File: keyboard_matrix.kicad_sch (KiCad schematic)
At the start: 208 parts

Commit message: Rename switch refdes
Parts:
- renumbered K_0 to SW2000, K_1 to SW2001, K_2 to SW2002, K_3 to SW2003, K_4 to SW2004, K_5 to SW2005, K_6 to SW2006, K_7 to SW2007, K_8 to SW2008, K_9 to SW2009, K_10 to SW2010, K_11 to SW2011, K_12 to SW2012, K_13 to SW2013, K_14 to SW2014, K_15 to SW2015, K_16 to SW2016, K_17 to SW2017, K_18 to SW2018, K_19 to SW2019, K_20 to SW2020, K_21 to SW2021, K_22 to SW2022, K_23 to SW2023, K_24 to SW2024, K_25 to SW2025, K_26 to SW2026, K_27 to SW2027, K_28 to SW2028, K_29 to SW2029, K_30 to SW2030, K_31 to SW2031, K_32 to SW2032, K_33 to SW2033, K_34 to SW2034, K_35 to SW2035, K_36 to SW2036, K_37 to SW2037, K_38 to SW2038, K_39 to SW2039, K_40 to SW2040, K_41 to SW2041, K_42 to SW2042, K_43 to SW2043, K_44 to SW2044, K_45 to SW2045, K_46 to SW2046, K_47 to SW2047, K_48 to SW2048, K_49 to SW2049, K_50 to SW2050, K_51 to SW2051, K_52 to SW2052, K_53 to SW2053, K_54 to SW2054, K_55 to SW2055, K_56 to SW2056, K_57 to SW2057, K_58 to SW2058, K_59 to SW2059, K_60 to SW2060, K_61 to SW2061, K_62 to SW2062, K_63 to SW2063, K_64 to SW2064, K_65 to SW2065, K_66 to SW2066, K_67 to SW2067, K_68 to SW2068, K_69 to SW2069, K_70 to SW2070, K_71 to SW2071, K_72 to SW2072, K_73 to SW2073, K_74 to SW2074, K_75 to SW2075, K_76 to SW2076, K_77 to SW2077, K_78 to SW2078, K_79 to SW2079, K_80 to SW2080, K_81 to SW2081, K_82 to SW2082, K_83 to SW2083, K_84 to SW2084, K_85 to SW2085, K_86 to SW2086, K_87 to SW2087, K_88 to SW2088, K_89 to SW2089, K_90 to SW2090, K_91 to SW2091, K_92 to SW2092, K_93 to SW2093, K_94 to SW2094, K_95 to SW2095, K_96 to SW2096, K_97 to SW2097, K_98 to SW2098, K_99 to SW2099, K_100 to SW2100, K_101 to SW2101, K_102 to SW2102, K_103 to SW2103

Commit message: Working towards SMD LEDs
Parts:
- added unit 2 of SW2000
- added SW? (x73): MX-LED, symbol Keyboard:MX-LED
- SW2000: value Esc -> MX-LED; footprint Keyboard:MXOnly-1U-Hotswap -> (none)
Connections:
- net G0: now also SW2000.4 (G), SW?.4 (G), SW?.4 (G), SW?.4 (G), SW?.4 (G), SW?.4 (G), SW?.4 (G), SW?.4 (G), SW?.4 (G), SW?.4 (G), SW?.4 (G), SW?.4 (G), SW?.4 (G), SW?.4 (G), SW?.4 (G), SW?.4 (G), SW?.4 (G), SW?.4 (G), SW?.4 (G), SW?.4 (G), SW?.4 (G), SW?.4 (G), SW?.4 (G), SW?.4 (G), SW?.4 (G), SW?.4 (G), SW?.4 (G), SW?.4 (G), SW?.4 (G), SW?.4 (G), SW?.4 (G), SW?.4 (G), SW?.4 (G), SW?.4 (G), SW?.4 (G), SW?.4 (G), SW?.4 (G), SW?.4 (G), SW?.4 (G), SW?.4 (G), SW?.4 (G), SW?.4 (G), SW?.4 (G), SW?.4 (G), SW?.4 (G), SW?.4 (G), SW?.4 (G), SW?.4 (G), SW?.4 (G), SW?.4 (G), SW?.4 (G), SW?.4 (G), SW?.4 (G), SW?.4 (G), SW?.4 (G), SW?.4 (G), SW?.4 (G), SW?.4 (G), SW?.4 (G), SW?.4 (G), SW?.4 (G), SW?.4 (G), SW?.4 (G), SW?.4 (G), SW?.4 (G), SW?.4 (G), SW?.4 (G), SW?.4 (G), SW?.4 (G), SW?.4 (G), SW?.4 (G), SW?.4 (G), SW?.4 (G), SW?.4 (G); no longer SW2000.4 (LEDGND)
- net LED36: no longer SW2036.3 (LED)
- net LED57: no longer SW2057.3 (LED)
- net LED90: no longer SW2090.3 (LED)
- net LED95: no longer SW2095.3 (LED)
- net row1: no longer D_17.1 (K)
- net row4: no longer D_74.1 (K)
- net row5: no longer D_92.1 (K)
- net at D_76.2 (A): no longer SW2076.2 (ROW)
- net at SW2019.2 (ROW): no longer D_19.2 (A)
- net at D_92.2 (A): no longer SW2092.2 (ROW)
- net at SW2074.2 (ROW): no longer D_74.2 (A)
- net at SW2059.2 (ROW): no longer D_59.2 (A)
- net at SW2018.2 (ROW): no longer D_18.2 (A)
- net at SW2038.2 (ROW): no longer D_38.2 (A)
- net at D_93.2 (A): no longer SW2093.2 (ROW)
- net at D_1.2 (A): no longer SW2001.2 (ROW)
- net at SW2017.2 (ROW): no longer D_17.2 (A)
- net at SW2039.2 (ROW): no longer D_39.2 (A)
- net at D_2.2 (A): no longer SW2002.2 (ROW)
- net at SW2060.2 (ROW): no longer D_60.2 (A)
- net at D_75.2 (A): no longer SW2075.2 (ROW)
- removed net G1: SW2001.4 (LEDGND)
- removed net G10: SW2010.4 (LEDGND)
- removed net G100: SW2100.4 (LEDGND)
- removed net G101: SW2101.4 (LEDGND)
- removed net G102: SW2102.4 (LEDGND)
- removed net G103: SW2103.4 (LEDGND)
- removed net G11: SW2011.4 (LEDGND)
- removed net G12: SW2012.4 (LEDGND)
- removed net G13: SW2013.4 (LEDGND)
- removed net G14: SW2014.4 (LEDGND)
- removed net G15: SW2015.4 (LEDGND)
- removed net G16: SW2016.4 (LEDGND)
- removed net G17: SW2017.4 (LEDGND)
- removed net G18: SW2018.4 (LEDGND)
- removed net G19: SW2019.4 (LEDGND)
- removed net G2: SW2002.4 (LEDGND)
- removed net G20: SW2020.4 (LEDGND)
- removed net G21: SW2021.4 (LEDGND)
- removed net G22: SW2022.4 (LEDGND)
- removed net G23: SW2023.4 (LEDGND)
- removed net G24: SW2024.4 (LEDGND)
- removed net G25: SW2025.4 (LEDGND)
- removed net G26: SW2026.4 (LEDGND)
- removed net G27: SW2027.4 (LEDGND)
- removed net G28: SW2028.4 (LEDGND)
- removed net G29: SW2029.4 (LEDGND)
- removed net G3: SW2003.4 (LEDGND)
- removed net G30: SW2030.4 (LEDGND)
- removed net G31: SW2031.4 (LEDGND)
- removed net G32: SW2032.4 (LEDGND)
- removed net G33: SW2033.4 (LEDGND)
- removed net G34: SW2034.4 (LEDGND)
- removed net G35: SW2035.4 (LEDGND)
- removed net G36: SW2036.4 (LEDGND)
- removed net G37: SW2037.4 (LEDGND)
- removed net G38: SW2038.4 (LEDGND)
- removed net G39: SW2039.4 (LEDGND)
- removed net G4: SW2004.4 (LEDGND)
- removed net G40: SW2040.4 (LEDGND)
- removed net G41: SW2041.4 (LEDGND)
- removed net G42: SW2042.4 (LEDGND)
- removed net G43: SW2043.4 (LEDGND)
- removed net G44: SW2044.4 (LEDGND)
- removed net G45: SW2045.4 (LEDGND)
- removed net G46: SW2046.4 (LEDGND)
- removed net G47: SW2047.4 (LEDGND)
- removed net G48: SW2048.4 (LEDGND)
- removed net G49: SW2049.4 (LEDGND)
- removed net G5: SW2005.4 (LEDGND)
- removed net G50: SW2050.4 (LEDGND)
- removed net G51: SW2051.4 (LEDGND)
- removed net G52: SW2052.4 (LEDGND)
- removed net G53: SW2053.4 (LEDGND)
- removed net G54: SW2054.4 (LEDGND)
- removed net G55: SW2055.4 (LEDGND)
- removed net G56: SW2056.4 (LEDGND)
- removed net G57: SW2057.4 (LEDGND)
- removed net G58: SW2058.4 (LEDGND)
- removed net G59: SW2059.4 (LEDGND)
- removed net G6: SW2006.4 (LEDGND)
- removed net G60: SW2060.4 (LEDGND)
- removed net G61: SW2061.4 (LEDGND)
- removed net G62: SW2062.4 (LEDGND)
- removed net G63: SW2063.4 (LEDGND)
- removed net G64: SW2064.4 (LEDGND)
- removed net G65: SW2065.4 (LEDGND)
- removed net G66: SW2066.4 (LEDGND)
- removed net G67: SW2067.4 (LEDGND)
- removed net G68: SW2068.4 (LEDGND)
- removed net G69: SW2069.4 (LEDGND)
- removed net G7: SW2007.4 (LEDGND)
- removed net G70: SW2070.4 (LEDGND)
- removed net G71: SW2071.4 (LEDGND)
- removed net G72: SW2072.4 (LEDGND)
- removed net G73: SW2073.4 (LEDGND)
- removed net G74: SW2074.4 (LEDGND)
- removed net G75: SW2075.4 (LEDGND)
- removed net G76: SW2076.4 (LEDGND)
- removed net G77: SW2077.4 (LEDGND)
- removed net G78: SW2078.4 (LEDGND)
- removed net G79: SW2079.4 (LEDGND)
- removed net G8: SW2008.4 (LEDGND)
- removed net G80: SW2080.4 (LEDGND)
- removed net G81: SW2081.4 (LEDGND)
- removed net G82: SW2082.4 (LEDGND)
- removed net G83: SW2083.4 (LEDGND)
- removed net G84: SW2084.4 (LEDGND)
- removed net G85: SW2085.4 (LEDGND)
- removed net G86: SW2086.4 (LEDGND)
- removed net G87: SW2087.4 (LEDGND)
- removed net G88: SW2088.4 (LEDGND)
- removed net G89: SW2089.4 (LEDGND)
- removed net G9: SW2009.4 (LEDGND)
- removed net G90: SW2090.4 (LEDGND)
- removed net G91: SW2091.4 (LEDGND)
- removed net G92: SW2092.4 (LEDGND)
- removed net G93: SW2093.4 (LEDGND)
- removed net G94: SW2094.4 (LEDGND)
- removed net G95: SW2095.4 (LEDGND)
- removed net G96: SW2096.4 (LEDGND)
- removed net G97: SW2097.4 (LEDGND)
- removed net G98: SW2098.4 (LEDGND)
- removed net G99: SW2099.4 (LEDGND)
- removed net LED0: SW2000.3 (LED)
- removed net LED1: SW2001.3 (LED)
- removed net LED10: SW2010.3 (LED)
- removed net LED100: SW2100.3 (LED)
- removed net LED101: SW2101.3 (LED)
- removed net LED102: SW2102.3 (LED)
- removed net LED103: SW2103.3 (LED)
- removed net LED11: SW2011.3 (LED)
- removed net LED12: SW2012.3 (LED)
- removed net LED13: SW2013.3 (LED)
- removed net LED14: SW2014.3 (LED)
- removed net LED15: SW2015.3 (LED)
- removed net LED16: SW2016.3 (LED)
- removed net LED17: SW2017.3 (LED)
- removed net LED18: SW2018.3 (LED)
- removed net LED19: SW2019.3 (LED)
- removed net LED2: SW2002.3 (LED)
- removed net LED20: SW2020.3 (LED)
- removed net LED21: SW2021.3 (LED)
- removed net LED22: SW2022.3 (LED)
- removed net LED23: SW2023.3 (LED)
- removed net LED24: SW2024.3 (LED)
- removed net LED25: SW2025.3 (LED)
- removed net LED26: SW2026.3 (LED)
- removed net LED27: SW2027.3 (LED)
- removed net LED28: SW2028.3 (LED)
- removed net LED29: SW2029.3 (LED)
- removed net LED3: SW2003.3 (LED)
- removed net LED30: SW2030.3 (LED)
- removed net LED31: SW2031.3 (LED)
- removed net LED32: SW2032.3 (LED)
- removed net LED33: SW2033.3 (LED)
- removed net LED34: SW2034.3 (LED)
- removed net LED35: SW2035.3 (LED)
- removed net LED37: SW2037.3 (LED)
- removed net LED38: SW2038.3 (LED)
- removed net LED39: SW2039.3 (LED)
- removed net LED4: SW2004.3 (LED)
- removed net LED40: SW2040.3 (LED)
- removed net LED41: SW2041.3 (LED)
- removed net LED42: SW2042.3 (LED)
- removed net LED43: SW2043.3 (LED)
- removed net LED44: SW2044.3 (LED)
- removed net LED45: SW2045.3 (LED)
- removed net LED46: SW2046.3 (LED)
- removed net LED47: SW2047.3 (LED)
- removed net LED48: SW2048.3 (LED)
- removed net LED49: SW2049.3 (LED)
- removed net LED5: SW2005.3 (LED)
- removed net LED50: SW2050.3 (LED)
- removed net LED51: SW2051.3 (LED)
- removed net LED52: SW2052.3 (LED)
- removed net LED53: SW2053.3 (LED)
- removed net LED54: SW2054.3 (LED)
- removed net LED55: SW2055.3 (LED)
- removed net LED56: SW2056.3 (LED)
- removed net LED58: SW2058.3 (LED)
- removed net LED59: SW2059.3 (LED)
- removed net LED6: SW2006.3 (LED)
- removed net LED60: SW2060.3 (LED)
- removed net LED61: SW2061.3 (LED)
- removed net LED62: SW2062.3 (LED)
- removed net LED63: SW2063.3 (LED)
- removed net LED64: SW2064.3 (LED)
- removed net LED65: SW2065.3 (LED)
- removed net LED66: SW2066.3 (LED)
- removed net LED67: SW2067.3 (LED)
- removed net LED68: SW2068.3 (LED)
- removed net LED69: SW2069.3 (LED)
- removed net LED7: SW2007.3 (LED)
- removed net LED70: SW2070.3 (LED)
- removed net LED71: SW2071.3 (LED)
- removed net LED72: SW2072.3 (LED)
- removed net LED73: SW2073.3 (LED)
- removed net LED74: SW2074.3 (LED)
- removed net LED75: SW2075.3 (LED)
- removed net LED76: SW2076.3 (LED)
- removed net LED77: SW2077.3 (LED)
- removed net LED78: SW2078.3 (LED)
- removed net LED79: SW2079.3 (LED)
- removed net LED8: SW2008.3 (LED)
- removed net LED80: SW2080.3 (LED)
- removed net LED81: SW2081.3 (LED)
- removed net LED82: SW2082.3 (LED)
- removed net LED83: SW2083.3 (LED)
- removed net LED84: SW2084.3 (LED)
- removed net LED85: SW2085.3 (LED)
- removed net LED86: SW2086.3 (LED)
- removed net LED87: SW2087.3 (LED)
- removed net LED88: SW2088.3 (LED)
- removed net LED89: SW2089.3 (LED)
- removed net LED9: SW2009.3 (LED)
- removed net LED91: SW2091.3 (LED)
- removed net LED92: SW2092.3 (LED)
- removed net LED93: SW2093.3 (LED)
- removed net LED94: SW2094.3 (LED)
- removed net LED96: SW2096.3 (LED)
- removed net LED97: SW2097.3 (LED)
- removed net LED98: SW2098.3 (LED)
- removed net LED99: SW2099.3 (LED)
- new net B0: SW2000.5 (B), SW?.5 (B), SW?.5 (B), SW?.5 (B), SW?.5 (B), SW?.5 (B), SW?.5 (B), SW?.5 (B), SW?.5 (B), SW?.5 (B), SW?.5 (B), SW?.5 (B), SW?.5 (B), SW?.5 (B), SW?.5 (B), SW?.5 (B), SW?.5 (B), SW?.5 (B), SW?.5 (B), SW?.5 (B), SW?.5 (B), SW?.5 (B), SW?.5 (B), SW?.5 (B), SW?.5 (B), SW?.5 (B), SW?.5 (B), SW?.5 (B), SW?.5 (B), SW?.5 (B), SW?.5 (B), SW?.5 (B), SW?.5 (B), SW?.5 (B), SW?.5 (B), SW?.5 (B), SW?.5 (B), SW?.5 (B), SW?.5 (B), SW?.5 (B), SW?.5 (B), SW?.5 (B), SW?.5 (B), SW?.5 (B), SW?.5 (B), SW?.5 (B), SW?.5 (B), SW?.5 (B), SW?.5 (B), SW?.5 (B), SW?.5 (B), SW?.5 (B), SW?.5 (B), SW?.5 (B), SW?.5 (B), SW?.5 (B), SW?.5 (B), SW?.5 (B), SW?.5 (B), SW?.5 (B), SW?.5 (B), SW?.5 (B), SW?.5 (B), SW?.5 (B), SW?.5 (B), SW?.5 (B), SW?.5 (B), SW?.5 (B), SW?.5 (B), SW?.5 (B), SW?.5 (B), SW?.5 (B), SW?.5 (B), SW?.5 (B)
- new net COM: SW2000.6 (COM), SW?.6 (COM), SW?.6 (COM), SW?.6 (COM), SW?.6 (COM), SW?.6 (COM), SW?.6 (COM), SW?.6 (COM), SW?.6 (COM), SW?.6 (COM), SW?.6 (COM), SW?.6 (COM), SW?.6 (COM), SW?.6 (COM), SW?.6 (COM), SW?.6 (COM), SW?.6 (COM), SW?.6 (COM), SW?.6 (COM), SW?.6 (COM), SW?.6 (COM), SW?.6 (COM), SW?.6 (COM), SW?.6 (COM), SW?.6 (COM), SW?.6 (COM), SW?.6 (COM), SW?.6 (COM), SW?.6 (COM), SW?.6 (COM), SW?.6 (COM), SW?.6 (COM), SW?.6 (COM), SW?.6 (COM), SW?.6 (COM), SW?.6 (COM), SW?.6 (COM), SW?.6 (COM), SW?.6 (COM), SW?.6 (COM), SW?.6 (COM), SW?.6 (COM), SW?.6 (COM), SW?.6 (COM), SW?.6 (COM), SW?.6 (COM), SW?.6 (COM), SW?.6 (COM), SW?.6 (COM), SW?.6 (COM), SW?.6 (COM), SW?.6 (COM), SW?.6 (COM), SW?.6 (COM), SW?.6 (COM), SW?.6 (COM), SW?.6 (COM), SW?.6 (COM), SW?.6 (COM), SW?.6 (COM), SW?.6 (COM), SW?.6 (COM), SW?.6 (COM), SW?.6 (COM), SW?.6 (COM), SW?.6 (COM), SW?.6 (COM), SW?.6 (COM), SW?.6 (COM), SW?.6 (COM), SW?.6 (COM), SW?.6 (COM), SW?.6 (COM), SW?.6 (COM)
- new net R0: SW2000.3 (R), SW?.3 (R), SW?.3 (R), SW?.3 (R), SW?.3 (R), SW?.3 (R), SW?.3 (R), SW?.3 (R), SW?.3 (R), SW?.3 (R), SW?.3 (R), SW?.3 (R), SW?.3 (R), SW?.3 (R), SW?.3 (R), SW?.3 (R), SW?.3 (R), SW?.3 (R), SW?.3 (R), SW?.3 (R), SW?.3 (R), SW?.3 (R), SW?.3 (R), SW?.3 (R), SW?.3 (R), SW?.3 (R), SW?.3 (R), SW?.3 (R), SW?.3 (R), SW?.3 (R), SW?.3 (R), SW?.3 (R), SW?.3 (R), SW?.3 (R), SW?.3 (R), SW?.3 (R), SW?.3 (R), SW?.3 (R), SW?.3 (R), SW?.3 (R), SW?.3 (R), SW?.3 (R), SW?.3 (R), SW?.3 (R), SW?.3 (R), SW?.3 (R), SW?.3 (R), SW?.3 (R), SW?.3 (R), SW?.3 (R), SW?.3 (R), SW?.3 (R), SW?.3 (R), SW?.3 (R), SW?.3 (R), SW?.3 (R), SW?.3 (R), SW?.3 (R), SW?.3 (R), SW?.3 (R), SW?.3 (R), SW?.3 (R), SW?.3 (R), SW?.3 (R), SW?.3 (R), SW?.3 (R), SW?.3 (R), SW?.3 (R), SW?.3 (R), SW?.3 (R), SW?.3 (R), SW?.3 (R), SW?.3 (R), SW?.3 (R)

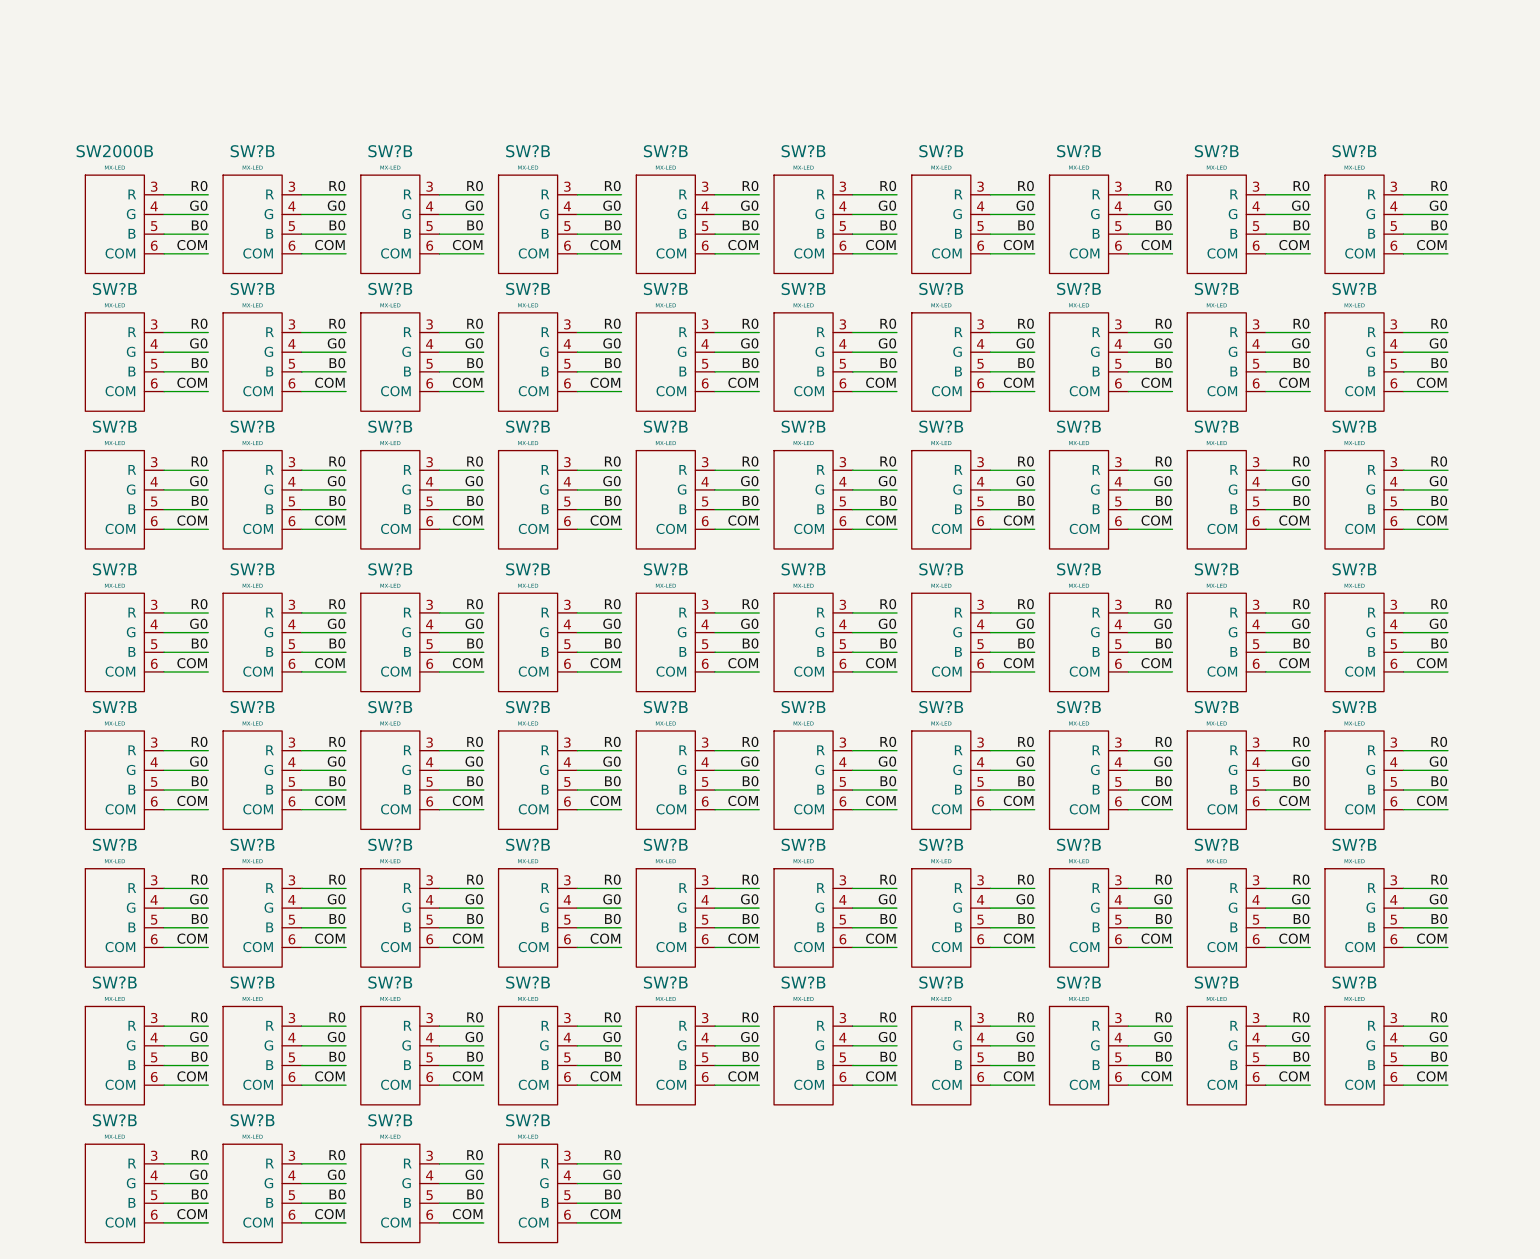
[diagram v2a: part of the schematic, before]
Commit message: Adding LED symbols
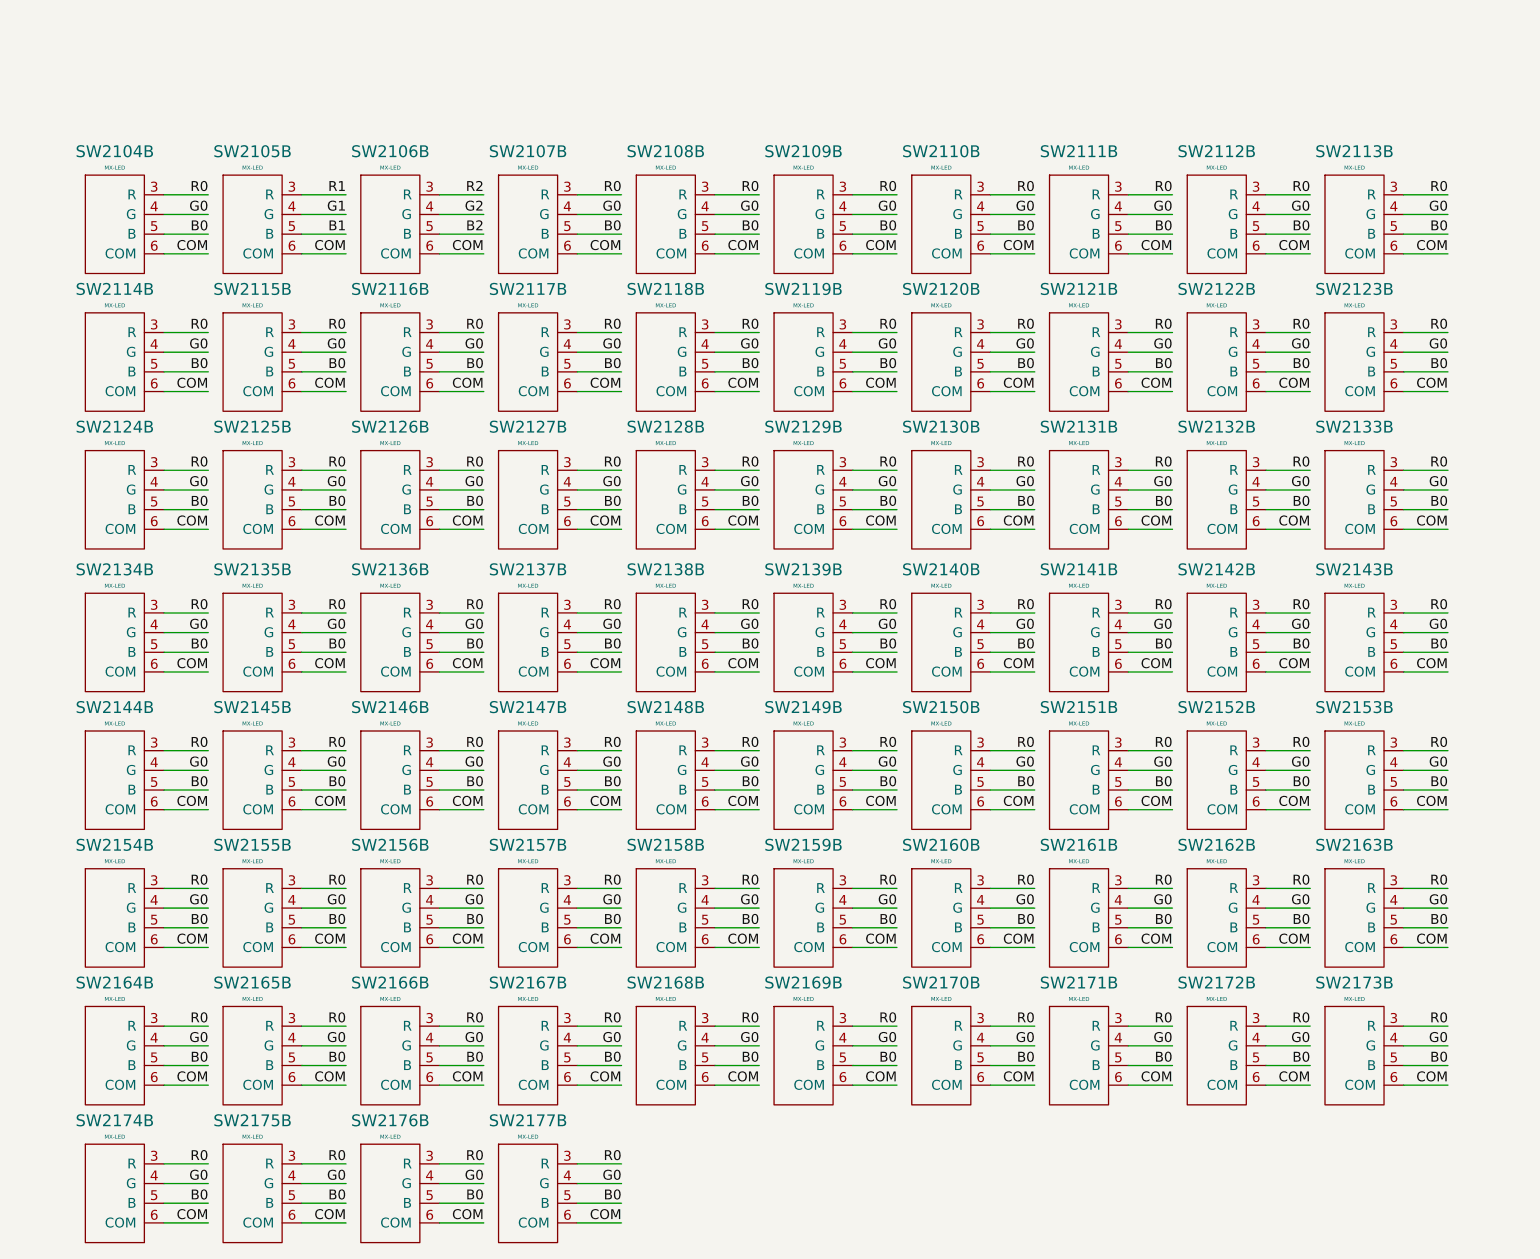
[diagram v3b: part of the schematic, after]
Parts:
- SW2001: value F1 -> MX-LED; footprint Keyboard:MXOnly-1U-Hotswap -> (none)
- gave numbers to parts that had none: 73
- renumbered SW2000 to SW2104
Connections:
- net B0: no longer SW2105.5 (B), SW2106.5 (B)
- net G0: no longer SW2105.4 (G), SW2106.4 (G)
- net R0: no longer SW2105.3 (R), SW2106.3 (R)
- new net B1: SW2105.5 (B)
- new net B2: SW2106.5 (B)
- new net G1: SW2105.4 (G)
- new net G2: SW2106.4 (G)
- new net R1: SW2105.3 (R)
- new net R2: SW2106.3 (R)
